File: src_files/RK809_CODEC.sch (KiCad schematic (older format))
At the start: 14 parts, among them U2 RK809

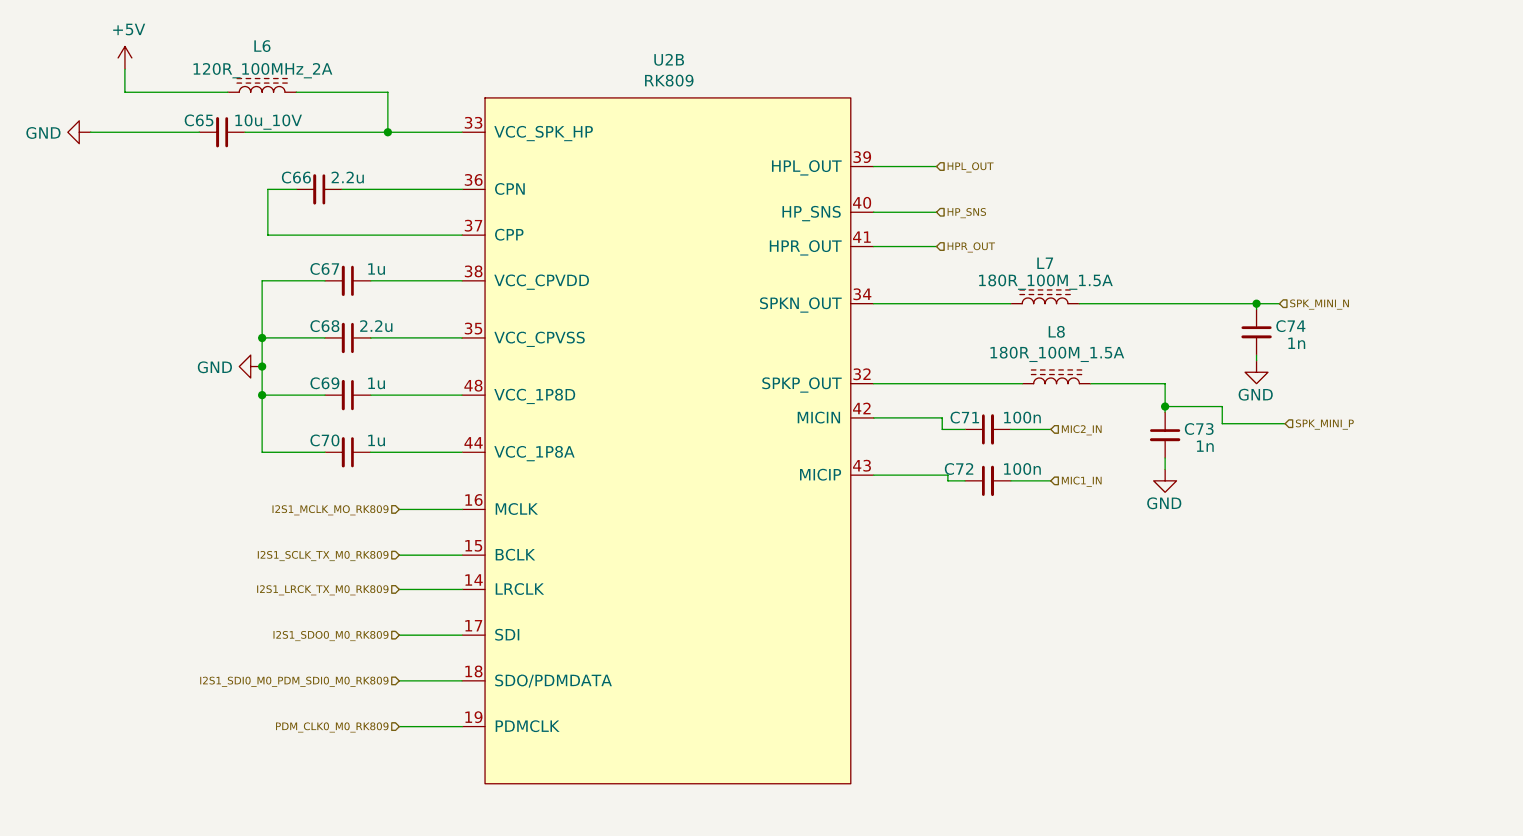
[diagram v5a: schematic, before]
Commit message: schematic capture complete
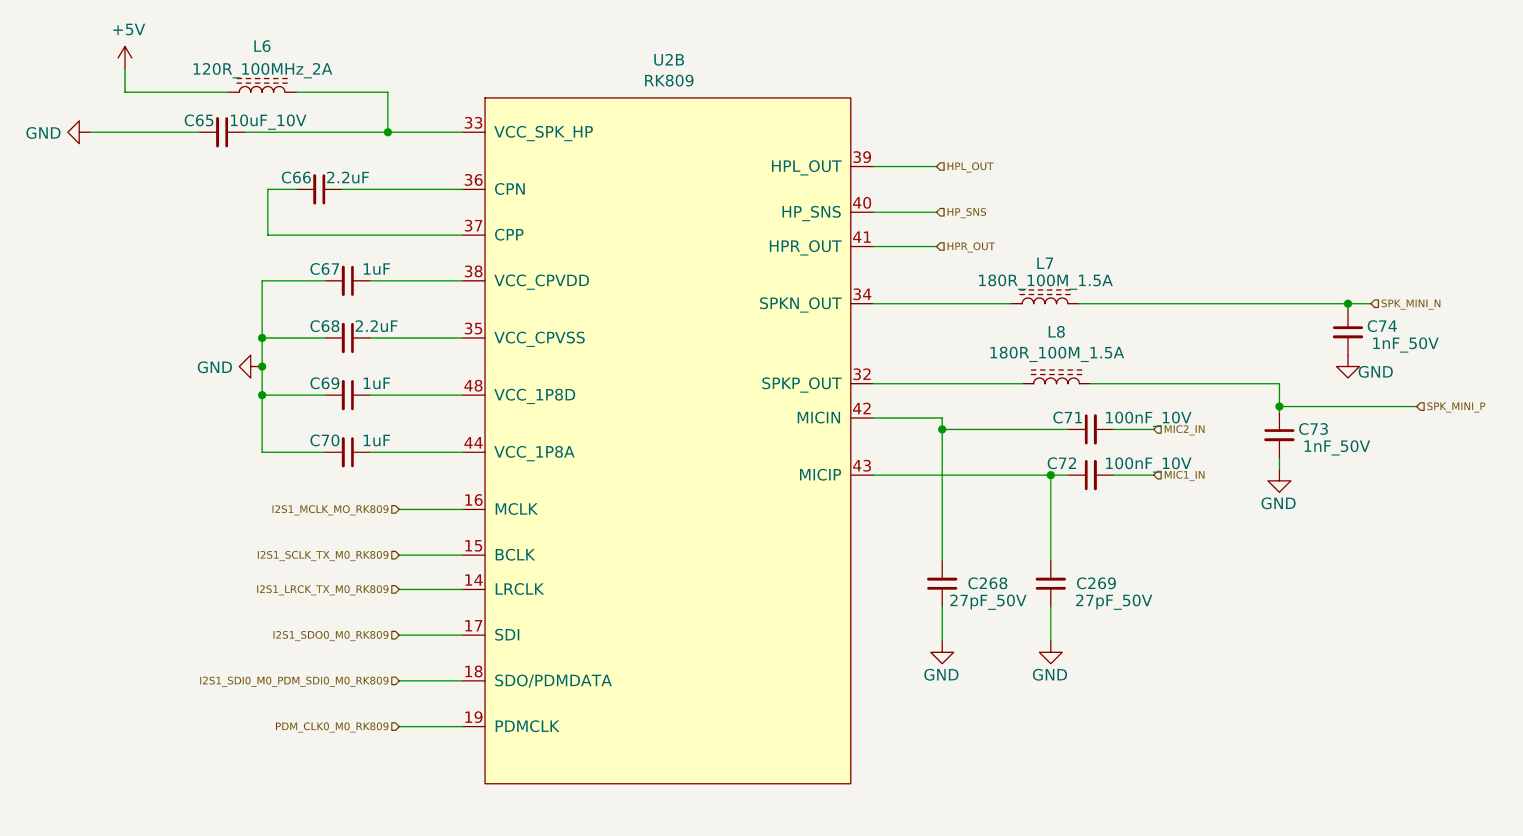
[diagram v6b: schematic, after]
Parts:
- added C268, C269: 27pF_50V, Capacitor_SMD:C_0402_1005Metric, symbol Device:C_Small
- C65: value 10u_10V -> 10uF_10V
- C66, C68: value 2.2u -> 2.2uF
- C67, C69, C70: value 1u -> 1uF
- C71, C72: value 100n -> 100nF_10V
- C73, C74: value 1n -> 1nF_50V
- L6: footprint Inductor_SMD:L_0805_2012Metric -> Inductor_SMD:L_0603_1608Metric; MPN (none) -> MPZ1608S121ATDH5
- L7, L8: footprint Inductor_SMD:L_0805_2012Metric -> Inductor_SMD:L_0603_1608Metric; MPN (none) -> 742792624
- U2: footprint (none) -> greencharge-footprints:QFN-68_EP_7x7_Pitch0.35mm
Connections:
- net GND: now also C268.1, C269.1
- net at C71.1, U2.42 (MICIN): now also C268.2
- net at C72.1, U2.43 (MICIP): now also C269.2
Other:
- moved on the sheet: C71, C72, C73, C74
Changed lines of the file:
@@
 $Descr A4 11693 8268
 encoding utf-8
-Sheet 5 13
+Sheet 4 15
 Title ""
 Date ""
@@
 P 3200 2000
 F 0 "C65" V 3150 1900 50  0000 C CNN
-F 1 "10u_10V" V 3150 2200 50  0000 C CNN
+F 1 "10uF_10V" V 3150 2200 50  0000 C CNN
 F 2 "Capacitor_SMD:C_0402_1005Metric" H 3200 2000 50  0001 C CNN
 F 3 "~" H 3200 2000 50  0001 C CNN
@@
 F 0 "L6" V 3575 1825 50  0000 C CNN
 F 1 "120R_100MHz_2A" V 3475 1825 50  0000 C CNN
-F 2 "Inductor_SMD:L_0805_2012Metric" H 3375 1825 50  0001 C CNN
+F 2 "Inductor_SMD:L_0603_1608Metric" H 3375 1825 50  0001 C CNN
 F 3 "~" H 3375 1825 50  0001 C CNN
+F 4 "MPZ1608S121ATDH5" V 3375 1825 50  0001 C CNN "MPN"
 	1    3375 1825
 	0    -1   -1   0
@@
 P 3750 2650
 F 0 "C67" V 3700 2550 50  0000 C CNN
-F 1 "1u" V 3700 2775 50  0000 C CNN
+F 1 "1uF" V 3700 2775 50  0000 C CNN
 F 2 "Capacitor_SMD:C_0402_1005Metric" H 3750 2650 50  0001 C CNN
 F 3 "~" H 3750 2650 50  0001 C CNN
@@
 F 0 "L7" V 6975 2750 50  0000 C CNN
 F 1 "180R_100M_1.5A" V 6900 2750 50  0000 C CNN
-F 2 "Inductor_SMD:L_0805_2012Metric" H 6800 2750 50  0001 C CNN
+F 2 "Inductor_SMD:L_0603_1608Metric" H 6800 2750 50  0001 C CNN
 F 3 "~" H 6800 2750 50  0001 C CNN
+F 4 "742792624" V 6800 2750 50  0001 C CNN "MPN"
 	1    6800 2750
 	0    -1   -1   0
@@
 F 0 "L8" V 7075 3100 50  0000 C CNN
 F 1 "180R_100M_1.5A" V 6984 3100 50  0000 C CNN
-F 2 "Inductor_SMD:L_0805_2012Metric" H 6850 3100 50  0001 C CNN
+F 2 "Inductor_SMD:L_0603_1608Metric" H 6850 3100 50  0001 C CNN
 F 3 "~" H 6850 3100 50  0001 C CNN
+F 4 "742792624" V 6850 3100 50  0001 C CNN "MPN"
 	1    6850 3100
 	0    -1   -1   0
@@
 L Device:C_Small C73
 U 1 1 621F3391
-P 7325 3325
-F 0 "C73" H 7475 3350 50  0000 C CNN
-F 1 "1n" H 7500 3275 50  0000 C CNN
-F 2 "Capacitor_SMD:C_0402_1005Metric" H 7325 3325 50  0001 C CNN
-F 3 "~" H 7325 3325 50  0001 C CNN
-	1    7325 3325
+P 7825 3325
+F 0 "C73" H 7975 3350 50  0000 C CNN
+F 1 "1nF_50V" H 8075 3275 50  0000 C CNN
+F 2 "Capacitor_SMD:C_0402_1005Metric" H 7825 3325 50  0001 C CNN
+F 3 "~" H 7825 3325 50  0001 C CNN
+	1    7825 3325
 	1    0    0    -1
 $EndComp
@@
 L Device:C_Small C74
 U 1 1 621F46DF
-P 7725 2875
-F 0 "C74" H 7875 2900 50  0000 C CNN
-F 1 "1n" H 7900 2825 50  0000 C CNN
-F 2 "Capacitor_SMD:C_0402_1005Metric" H 7725 2875 50  0001 C CNN
-F 3 "~" H 7725 2875 50  0001 C CNN
-	1    7725 2875
+P 8125 2875
+F 0 "C74" H 8275 2900 50  0000 C CNN
+F 1 "1nF_50V" H 8375 2825 50  0000 C CNN
+F 2 "Capacitor_SMD:C_0402_1005Metric" H 8125 2875 50  0001 C CNN
+F 3 "~" H 8125 2875 50  0001 C CNN
+	1    8125 2875
 	1    0    0    -1
 $EndComp
@@
 	6050 3100 6700 3100
 Wire Wire Line
-	7725 2775 7725 2750
-Wire Wire Line
-	7725 2750 6950 2750
+	8125 2775 8125 2750
+Wire Wire Line
+	8125 2750 6950 2750
 Wire Wire Line
 	6650 2750 6050 2750
@@
 L OLIMEX_Power:GND #PWR0172
 U 1 1 621F828D
-P 7725 3000
-F 0 "#PWR0172" H 7725 2750 50  0001 C CNN
-F 1 "GND" H 7800 2850 50  0000 R CNN
-F 2 "" H 7725 3000 60  0000 C CNN
-F 3 "" H 7725 3000 60  0000 C CNN
-	1    7725 3000
-	1    0    0    -1
-$EndComp
-Wire Wire Line
-	7325 3425 7325 3475
-Text HLabel 7825 2750 2    33   Input ~ 0
+P 8125 2975
+F 0 "#PWR0172" H 8125 2725 50  0001 C CNN
+F 1 "GND" H 8325 2900 50  0000 R CNN
+F 2 "" H 8125 2975 60  0000 C CNN
+F 3 "" H 8125 2975 60  0000 C CNN
+	1    8125 2975
+	1    0    0    -1
+$EndComp
+Wire Wire Line
+	7825 3425 7825 3475
+Text HLabel 8225 2750 2    33   Input ~ 0
 SPK_MINI_N
-Text HLabel 7850 3275 2    33   Input ~ 0
+Text HLabel 8425 3200 2    33   Input ~ 0
 SPK_MINI_P
-Wire Wire Line
-	7725 3000 7725 2975
 $Comp
 L OLIMEX_Power:GND #PWR0173
 U 1 1 621FEADE
-P 7325 3475
-F 0 "#PWR0173" H 7325 3225 50  0001 C CNN
-F 1 "GND" H 7400 3325 50  0000 R CNN
-F 2 "" H 7325 3475 60  0000 C CNN
-F 3 "" H 7325 3475 60  0000 C CNN
-	1    7325 3475
-	1    0    0    -1
-$EndComp
-Wire Wire Line
-	7825 2750 7725 2750
-Connection ~ 7725 2750
-Wire Wire Line
-	7000 3100 7325 3100
-Wire Wire Line
-	7325 3200 7575 3200
-Wire Wire Line
-	7575 3200 7575 3275
-Wire Wire Line
-	7575 3275 7850 3275
-Wire Wire Line
-	7325 3100 7325 3200
-Connection ~ 7325 3200
-Wire Wire Line
-	7325 3200 7325 3225
+P 7825 3475
+F 0 "#PWR0173" H 7825 3225 50  0001 C CNN
+F 1 "GND" H 7900 3325 50  0000 R CNN
+F 2 "" H 7825 3475 60  0000 C CNN
+F 3 "" H 7825 3475 60  0000 C CNN
+	1    7825 3475
+	1    0    0    -1
+$EndComp
+Wire Wire Line
+	8225 2750 8125 2750
+Connection ~ 8125 2750
+Wire Wire Line
+	7000 3100 7825 3100
+Wire Wire Line
+	7825 3100 7825 3200
+Connection ~ 7825 3200
+Wire Wire Line
+	7825 3200 7825 3225
 $Comp
 L Device:C_Small C71
 U 1 1 62204B09
-P 6550 3300
-F 0 "C71" V 6600 3400 50  0000 C CNN
-F 1 "100n" V 6600 3150 50  0000 C CNN
-F 2 "Capacitor_SMD:C_0402_1005Metric" H 6550 3300 50  0001 C CNN
-F 3 "~" H 6550 3300 50  0001 C CNN
-	1    6550 3300
+P 7000 3300
+F 0 "C71" V 7050 3400 50  0000 C CNN
+F 1 "100nF_10V" V 7050 3050 50  0000 C CNN
+F 2 "Capacitor_SMD:C_0402_1005Metric" H 7000 3300 50  0001 C CNN
+F 3 "~" H 7000 3300 50  0001 C CNN
+	1    7000 3300
 	0    -1   -1   0
 $EndComp
@@
 L Device:C_Small C72
 U 1 1 622058C7
-P 6550 3525
-F 0 "C72" V 6600 3650 50  0000 C CNN
-F 1 "100n" V 6600 3375 50  0000 C CNN
-F 2 "Capacitor_SMD:C_0402_1005Metric" H 6550 3525 50  0001 C CNN
-F 3 "~" H 6550 3525 50  0001 C CNN
-	1    6550 3525
+P 7000 3500
+F 0 "C72" V 7050 3625 50  0000 C CNN
+F 1 "100nF_10V" V 7050 3250 50  0000 C CNN
+F 2 "Capacitor_SMD:C_0402_1005Metric" H 7000 3500 50  0001 C CNN
+F 3 "~" H 7000 3500 50  0001 C CNN
+	1    7000 3500
 	0    -1   -1   0
 $EndComp
@@
 	6350 3250 6350 3300
 Wire Wire Line
-	6350 3300 6450 3300
-Wire Wire Line
-	6050 3500 6375 3500
-Wire Wire Line
-	6375 3500 6375 3525
-Wire Wire Line
-	6375 3525 6450 3525
-Wire Wire Line
-	6650 3300 6825 3300
-Wire Wire Line
-	6650 3525 6825 3525
-Text HLabel 6825 3525 2    33   Input ~ 0
+	6350 3300 6900 3300
+Wire Wire Line
+	7100 3300 7275 3300
+Wire Wire Line
+	7100 3500 7275 3500
+Text HLabel 7275 3500 2    33   Input ~ 0
 MIC1_IN
-Text HLabel 6825 3300 2    33   Input ~ 0
+Text HLabel 7275 3300 2    33   Input ~ 0
 MIC2_IN
 Wire Wire Line
@@
 P 3750 3400
 F 0 "C70" V 3700 3300 50  0000 C CNN
-F 1 "1u" V 3700 3525 50  0000 C CNN
+F 1 "1uF" V 3700 3525 50  0000 C CNN
 F 2 "Capacitor_SMD:C_0402_1005Metric" H 3750 3400 50  0001 C CNN
 F 3 "~" H 3750 3400 50  0001 C CNN
@@
 P 3750 3150
 F 0 "C69" V 3700 3050 50  0000 C CNN
-F 1 "1u" V 3700 3275 50  0000 C CNN
+F 1 "1uF" V 3700 3275 50  0000 C CNN
 F 2 "Capacitor_SMD:C_0402_1005Metric" H 3750 3150 50  0001 C CNN
 F 3 "~" H 3750 3150 50  0001 C CNN
@@
 P 3750 2900
 F 0 "C68" V 3700 2800 50  0000 C CNN
-F 1 "2.2u" V 3700 3025 50  0000 C CNN
+F 1 "2.2uF" V 3700 3025 50  0000 C CNN
 F 2 "Capacitor_SMD:C_0402_1005Metric" H 3750 2900 50  0001 C CNN
 F 3 "~" H 3750 2900 50  0001 C CNN
@@
 P 3625 2250
 F 0 "C66" V 3575 2150 50  0000 C CNN
-F 1 "2.2u" V 3575 2375 50  0000 C CNN
+F 1 "2.2uF" V 3575 2375 50  0000 C CNN
 F 2 "Capacitor_SMD:C_0402_1005Metric" H 3625 2250 50  0001 C CNN
 F 3 "~" H 3625 2250 50  0001 C CNN
@@
 F 0 "U2" H 5155 1915 50  0000 C CNN
 F 1 "RK809" H 5155 1824 50  0000 C CNN
-F 2 "" H 5150 2000 50  0001 C CNN
+F 2 "greencharge-footprints:QFN-68_EP_7x7_Pitch0.35mm" H 5150 2000 50  0001 C CNN
 F 3 "" H 5150 2000 50  0001 C CNN
 	2    5250 1800
 	1    0    0    -1
 $EndComp
+$Comp
+L Device:C_Small C269
+U 1 1 627E7AFD
+P 6825 3975
+F 0 "C269" H 6625 3975 50  0000 C CNN
+F 1 "27pF_50V" H 6550 4050 50  0000 C CNN
+F 2 "Capacitor_SMD:C_0402_1005Metric" H 6825 3975 50  0001 C CNN
+F 3 "~" H 6825 3975 50  0001 C CNN
+	1    6825 3975
+	-1   0    0    1
+$EndComp
+$Comp
+L Device:C_Small C268
+U 1 1 627EB531
+P 6350 3975
+F 0 "C268" H 6150 3975 50  0000 C CNN
+F 1 "27pF_50V" H 6150 4050 50  0000 C CNN
+F 2 "Capacitor_SMD:C_0402_1005Metric" H 6350 3975 50  0001 C CNN
+F 3 "~" H 6350 3975 50  0001 C CNN
+	1    6350 3975
+	-1   0    0    1
+$EndComp
+Wire Wire Line
+	6350 3875 6350 3300
+Connection ~ 6350 3300
+Wire Wire Line
+	6825 3875 6825 3500
+$Comp
+L OLIMEX_Power:GND #PWR0202
+U 1 1 627F02EB
+P 6350 4225
+F 0 "#PWR0202" H 6350 3975 50  0001 C CNN
+F 1 "GND" H 6425 4075 50  0000 R CNN
+F 2 "" H 6350 4225 60  0000 C CNN
+F 3 "" H 6350 4225 60  0000 C CNN
+	1    6350 4225
+	1    0    0    -1
+$EndComp
+$Comp
+L OLIMEX_Power:GND #PWR0203
+U 1 1 627F1A88
+P 6825 4225
+F 0 "#PWR0203" H 6825 3975 50  0001 C CNN
+F 1 "GND" H 6900 4075 50  0000 R CNN
+F 2 "" H 6825 4225 60  0000 C CNN
+F 3 "" H 6825 4225 60  0000 C CNN
+	1    6825 4225
+	1    0    0    -1
+$EndComp
+Wire Wire Line
+	6825 4225 6825 4075
+Wire Wire Line
+	6350 4225 6350 4075
+Connection ~ 6825 3500
+Wire Wire Line
+	6825 3500 6900 3500
+Wire Wire Line
+	7825 3200 8425 3200
+Wire Wire Line
+	6050 3500 6825 3500
 $EndSCHEMATC
